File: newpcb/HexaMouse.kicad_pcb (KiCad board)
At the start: 2 copper layers, 56 x 63.5 mm, 23 parts, among them J1 Conn_01x02_Pin, J2 Conn_01x02_Pin, SW1 SW_SPDT, SW2 SW_Push, SW3 SW_Push, U1 XIAO-Add-On, U2 MLX90393SLW-ABA-011-RE, U3 MLX90393SLW-ABA-011-RE, U4 MLX90393SLW-ABA-011-RE

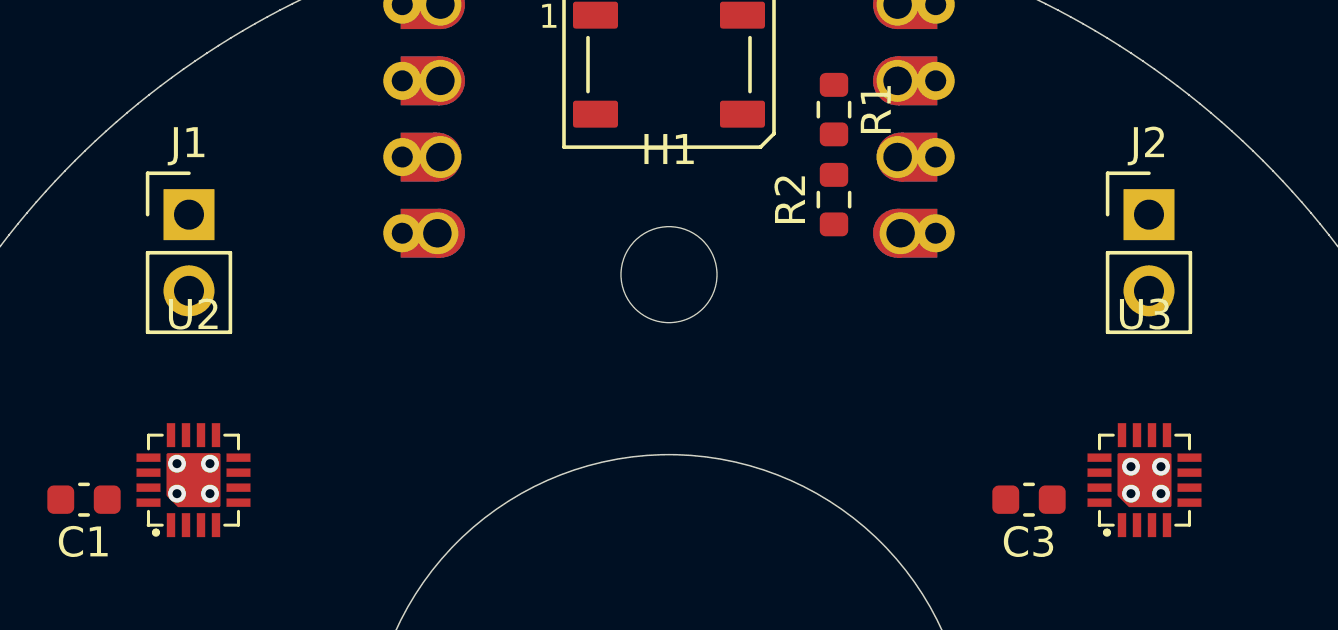
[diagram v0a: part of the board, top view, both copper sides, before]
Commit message: Swapped battery nets
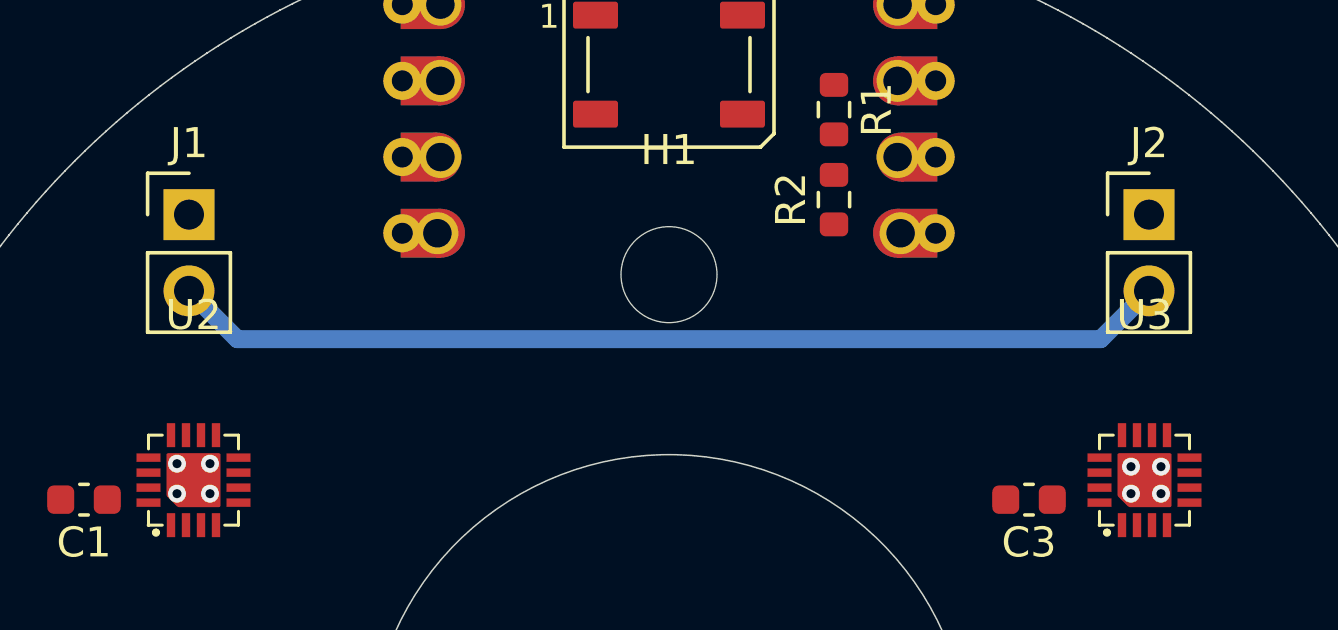
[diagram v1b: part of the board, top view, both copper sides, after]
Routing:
- net Net-(J1-Pin_2): track 0.00 -> 33.3 mm
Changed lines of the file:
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@@
 		(net "GND")
+	)
+	(segment
+		(start 134 84.54)
+		(end 135.61 86.15)
+		(width 0.6)
+		(layer "B.Cu")
+		(net "Net-(J1-Pin_2)")
+	)
+	(segment
+		(start 135.61 86.15)
+		(end 164.39 86.15)
+		(width 0.6)
+		(layer "B.Cu")
+		(net "Net-(J1-Pin_2)")
+	)
+	(segment
+		(start 164.39 86.15)
+		(end 166 84.54)
+		(width 0.6)
+		(layer "B.Cu")
+		(net "Net-(J1-Pin_2)")
 	)
 	(zone

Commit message: Did some routing
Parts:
- moved J1 32.1 mm to (166.0, 85.0), turned to 180 degrees
- moved J2 32.1 mm to (134.0, 85.0), turned to 180 degrees
- moved R3 1.12 mm to (153.0, 73.5), turned to 180 degrees
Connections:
- J2 pad 1: Net-(J2-Pin_1) -> Net-(J1-Pin_1)
- J2 pad 2: Net-(J1-Pin_2) -> Net-(J2-Pin_2)
- SW1 pad 2: Net-(J1-Pin_1) -> Net-(J1-Pin_2)
- SW1 pad 3: Net-(J2-Pin_1) -> Net-(J2-Pin_2)
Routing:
- net +3.3V: track 0.00 -> 163.6 mm, vias 0 -> 4
- net SW2: track 0.00 -> 53.0 mm, vias 0 -> 2
- net SW1: track 0.00 -> 47.8 mm, vias 0 -> 1
- net Net-(D1-DOUT): track 0.00 -> 39.9 mm
- net Net-(D2-DOUT): track 0.00 -> 38.1 mm
- net Net-(J1-Pin_1): track 0.00 -> 33.0 mm
- net Net-(J2-Pin_2): track 0.00 -> 31.7 mm, vias 0 -> 1
- net SDA: track 0.00 -> 22.2 mm
- net GND: track 0.00 -> 19.4 mm, vias 12 -> 16
- net LED-DATA: track 0.00 -> 4.42 mm
- net SCL: track 0.00 -> 2.37 mm
- net Net-(D1-DIN): track 0.00 -> 1.96 mm
- net Net-(J1-Pin_2): track 33.3 -> 31.9 mm, vias 0 -> 1

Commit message: did some routing
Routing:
- net SCL: track 2.37 -> 123.8 mm, vias 0 -> 5
- net SDA: track 22.2 -> 59.4 mm, vias 0 -> 2

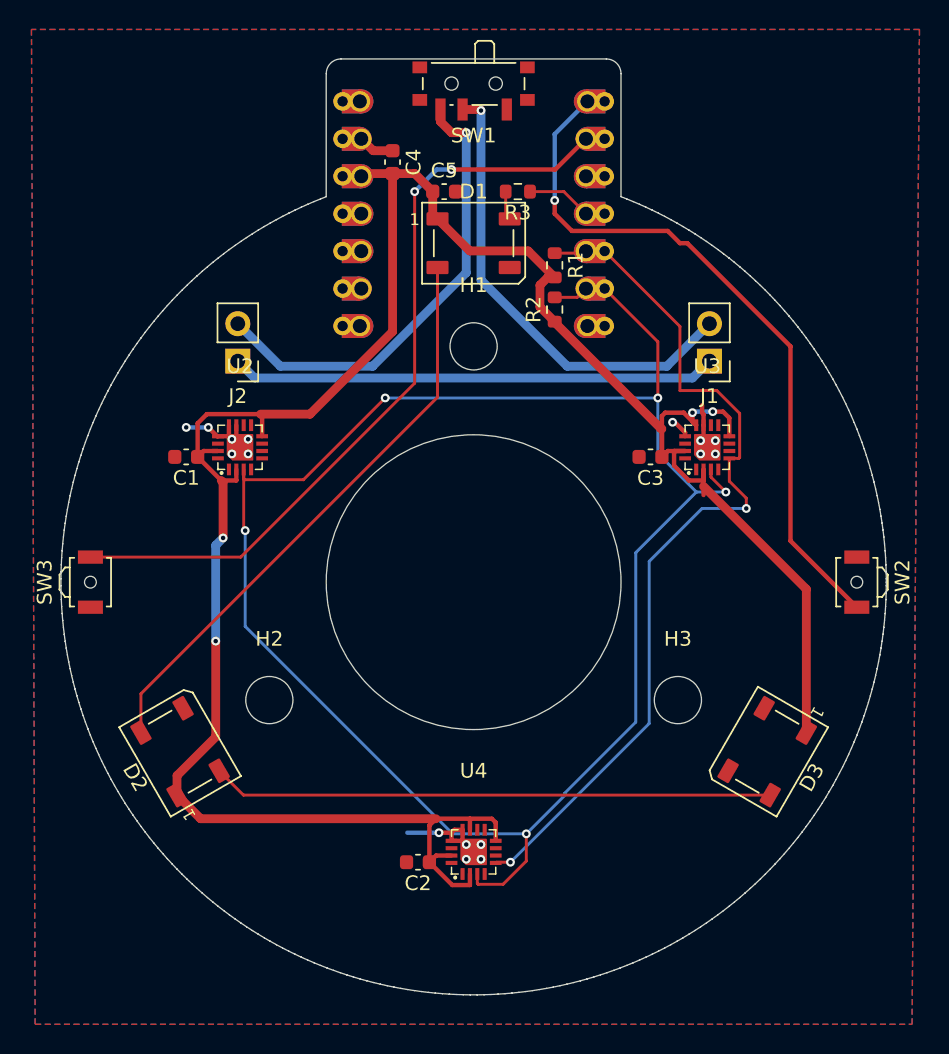
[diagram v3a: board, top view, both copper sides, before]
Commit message: Solved some drc errors
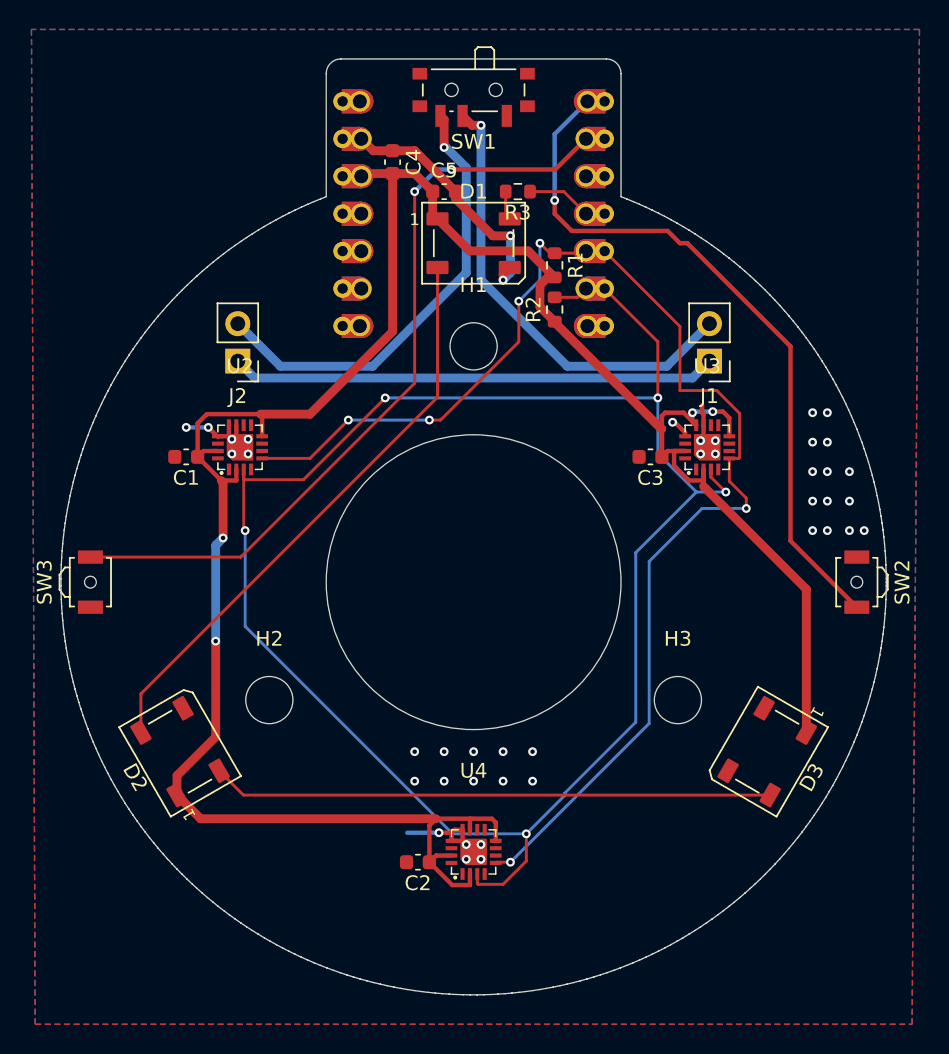
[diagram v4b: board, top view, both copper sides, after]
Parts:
- moved SW1 0.43 mm to (150.0, 66.9)
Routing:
- net SDA: track 59.4 -> 88.7 mm, vias 2 -> 6
- net GND: track 19.4 -> 34.4 mm, vias 16 -> 42
- net Net-(J1-Pin_2): track 31.9 -> 31.1 mm

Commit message: Started on some silkscreen
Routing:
- net GND: vias 42 -> 152
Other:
- board text added: "Designed by Hugo H"
- board text added: "HexaMouse"
- board text added: "https://github.com/hhhug000/HexaMouse"
- board text added: "v1.0"
